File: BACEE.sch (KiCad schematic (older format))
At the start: 8 parts

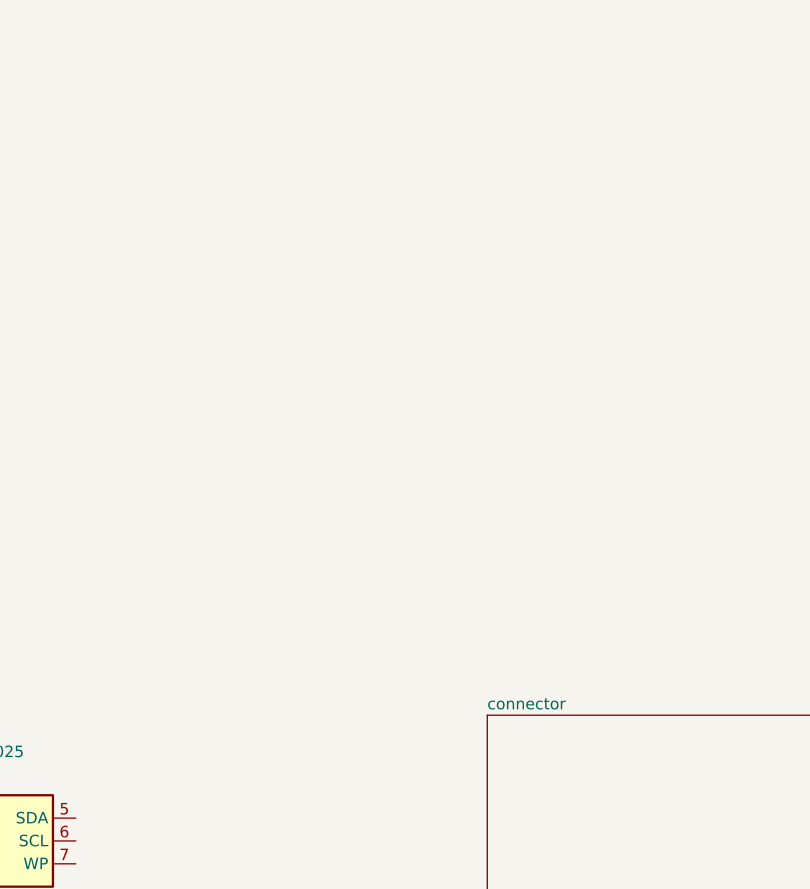
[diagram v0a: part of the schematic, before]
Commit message: created a new symbol
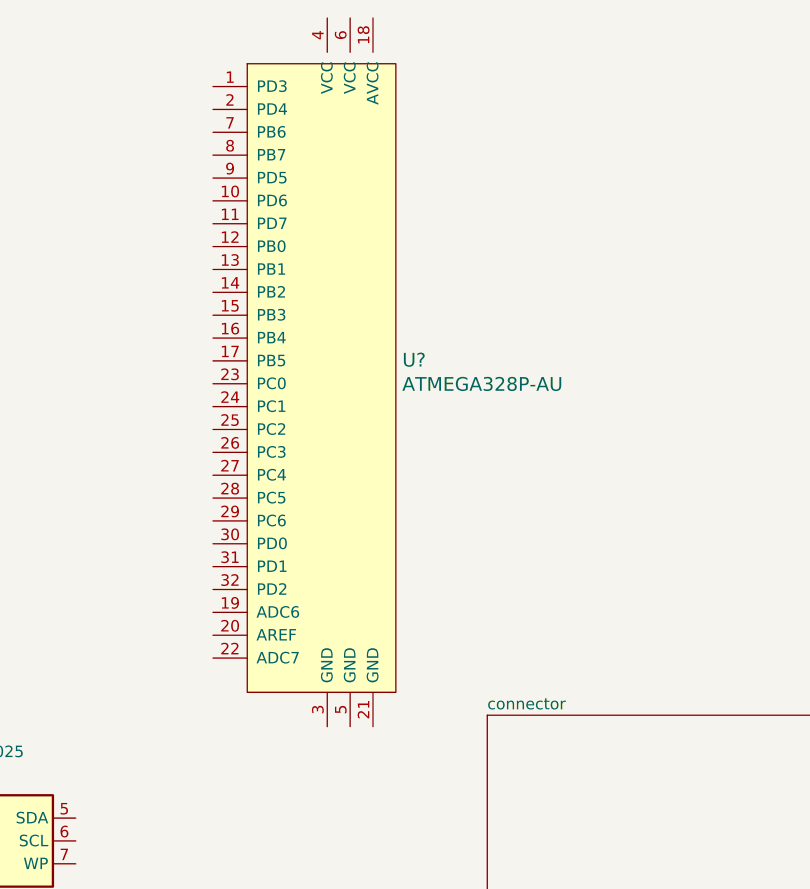
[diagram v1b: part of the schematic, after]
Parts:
- added U?: ATMEGA328P-AU, digikey-footprints:TQFP-32_7x7mm, symbol dk_Embedded-Microcontrollers:ATMEGA328P-AU
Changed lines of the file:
@@
 F1 "Connectors1.sch" 50
 $EndSheet
+$Comp
+L dk_Embedded-Microcontrollers:ATMEGA328P-AU U?
+U 1 1 5EFBB5FA
+P 7650 1750
+F 0 "U?" H 7978 1853 60  0000 L CNN
+F 1 "ATMEGA328P-AU" H 7978 1747 60  0000 L CNN
+F 2 "digikey-footprints:TQFP-32_7x7mm" H 7850 1950 60  0001 L CNN
+F 3 "http://www.microchip.com/mymicrochip/filehandler.aspx?ddocname=en608326" H 7850 2050 60  0001 L CNN
+F 4 "ATMEGA328P-AU-ND" H 7850 2150 60  0001 L CNN "Digi-Key_PN"
+F 5 "ATMEGA328P-AU" H 7850 2250 60  0001 L CNN "MPN"
+F 6 "Integrated Circuits (ICs)" H 7850 2350 60  0001 L CNN "Category"
+F 7 "Embedded - Microcontrollers" H 7850 2450 60  0001 L CNN "Family"
+F 8 "http://www.microchip.com/mymicrochip/filehandler.aspx?ddocname=en608326" H 7850 2550 60  0001 L CNN "DK_Datasheet_Link"
+F 9 "/product-detail/en/microchip-technology/ATMEGA328P-AU/ATMEGA328P-AU-ND/1832260" H 7850 2650 60  0001 L CNN "DK_Detail_Page"
+F 10 "IC MCU 8BIT 32KB FLASH 32TQFP" H 7850 2750 60  0001 L CNN "Description"
+F 11 "Microchip Technology" H 7850 2850 60  0001 L CNN "Manufacturer"
+F 12 "Active" H 7850 2950 60  0001 L CNN "Status"
+	1    7650 1750
+	1    0    0    -1
+$EndComp
 $EndSCHEMATC

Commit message: wiring done ... no DRC errors
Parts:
- added U2: 24LC1025, Package_SO:SOIJ-8_5.3x5.3mm_P1.27mm, symbol Memory_EEPROM:24LC1025
- added U3: DS1337_KTH, Package_SO:SO-8_5.3x6.2mm_P1.27mm, symbol Project_3_custom:DS1337_KTH
- added Y1: Crystal 32MHz, Crystal:Crystal_SMD_MicroCrystal_CC7V-T1A-2Pin_3.2x1.5mm, symbol Device:Crystal
- added Y2: Crystal 16MHz, Crystal:Crystal_SMD_5032-2Pin_5.0x3.2mm_HandSoldering, symbol Device:Crystal
- BT1: renamed from BT?; value Battery -> 3V; footprint (none) -> Connector_PinHeader_2.54mm:PinHeader_1x02_P2.54mm_Vertical
- C1, C2: renamed from C?; value C -> 22pF; footprint (none) -> Capacitor_SMD:C_0805_2012Metric_Pad1.15x1.40mm_HandSolder
- C3: renamed from C?; value CP -> 10uF; footprint (none) -> Capacitor_SMD:C_0805_2012Metric_Pad1.15x1.40mm_HandSolder
- D1: renamed from D?; footprint (none) -> LED_SMD:LED_0805_2012Metric_Pad1.15x1.40mm_HandSolder
- R1: renamed from R?; value R -> 330 ohms; footprint (none) -> Resistor_SMD:R_0805_2012Metric_Pad1.15x1.40mm_HandSolder
- R2: renamed from R?; value R -> 10k ohms; footprint (none) -> Resistor_SMD:R_0805_2012Metric_Pad1.15x1.40mm_HandSolder
- U1: renamed from U?; footprint (none) -> Package_SO:SOIJ-8_5.3x5.3mm_P1.27mm
- gave numbers to parts that had none: 1
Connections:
- net VCC: now reaches BT1.1 (+)
- net VCC: now also C3.1, R2.1, U1.3 (A2), U1.8 (VCC), U4.18 (AVCC), U4.20 (AREF), U4.4 (VCC), U4.6 (VCC), U2.3 (A2), U2.8 (VCC), U3.3 (INTA), U3.8 (Vcc)
- net GND: now reaches BT1.2 (-)
- net GND: now also C1.2, C2.2, C3.2, R1.2, U1.4 (GND), U1.7 (WP), U4.21 (GND), U4.3 (GND), U4.5 (GND), U2.4 (GND), U2.7 (WP), U3.4 (GND)
- net at C1.1: now also U4.7 (PB6), Y2.1
- net at C2.1: now also U4.8 (PB7), Y2.2
- net at D1.1 (K): now also R1.1
- net at D1.2 (A): now also U4.17 (PB5)
- net RST: now reaches R2.2
- net RST: now also U4.29 (PC6)
- net ADDS1: now reaches U1.1 (A0)
- net ADDS1: now also U4.23 (PC0), U2.1 (A0)
- net ADDS2: now reaches U1.2 (A1)
- net ADDS2: now also U4.24 (PC1), U2.2 (A1)
- net SDA: now reaches U1.5 (SDA)
- net SDA: now also U4.27 (PC4), U2.5 (SDA), U3.5 (SDA)
- net SCK: now reaches U1.6 (SCL)
- net SCK: now also U4.28 (PC5), U2.6 (SCL), U3.6 (SCL)
- net D3: now reaches U4.1 (PD3)
- net D6: now reaches U4.10 (PD6)
- net D7: now reaches U4.11 (PD7)
- net D8: now reaches U4.12 (PB0)
- net MOSI: now reaches U4.15 (PB3)
- net MISO: now reaches U4.16 (PB4)
- net D4: now reaches U4.2 (PD4)
- net RX: now reaches U4.30 (PD0)
- net TX: now reaches U4.31 (PD1)
- net D2: now reaches U4.32 (PD2)
- net D5: now reaches U4.9 (PD5)
- new net: U3.1 (X1), Y1.1
- new net: U3.2 (X2), Y1.2
- no-connect marks 0 -> 7
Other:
- moved on the sheet: BT1, C1, C2, C3, D1, R1, R2, U1, U4

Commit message: comments and netlist
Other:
- note added: "ATMEGA328P-AU with Oscilaltor and Battery"
- note added: "Clock/calender"
- note added: "Connectors"
- note added: "EPROM"
- moved on the sheet: BT1, C1, C2, C3, D1, R1, R2, U1, U2, U3, U4, Y1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

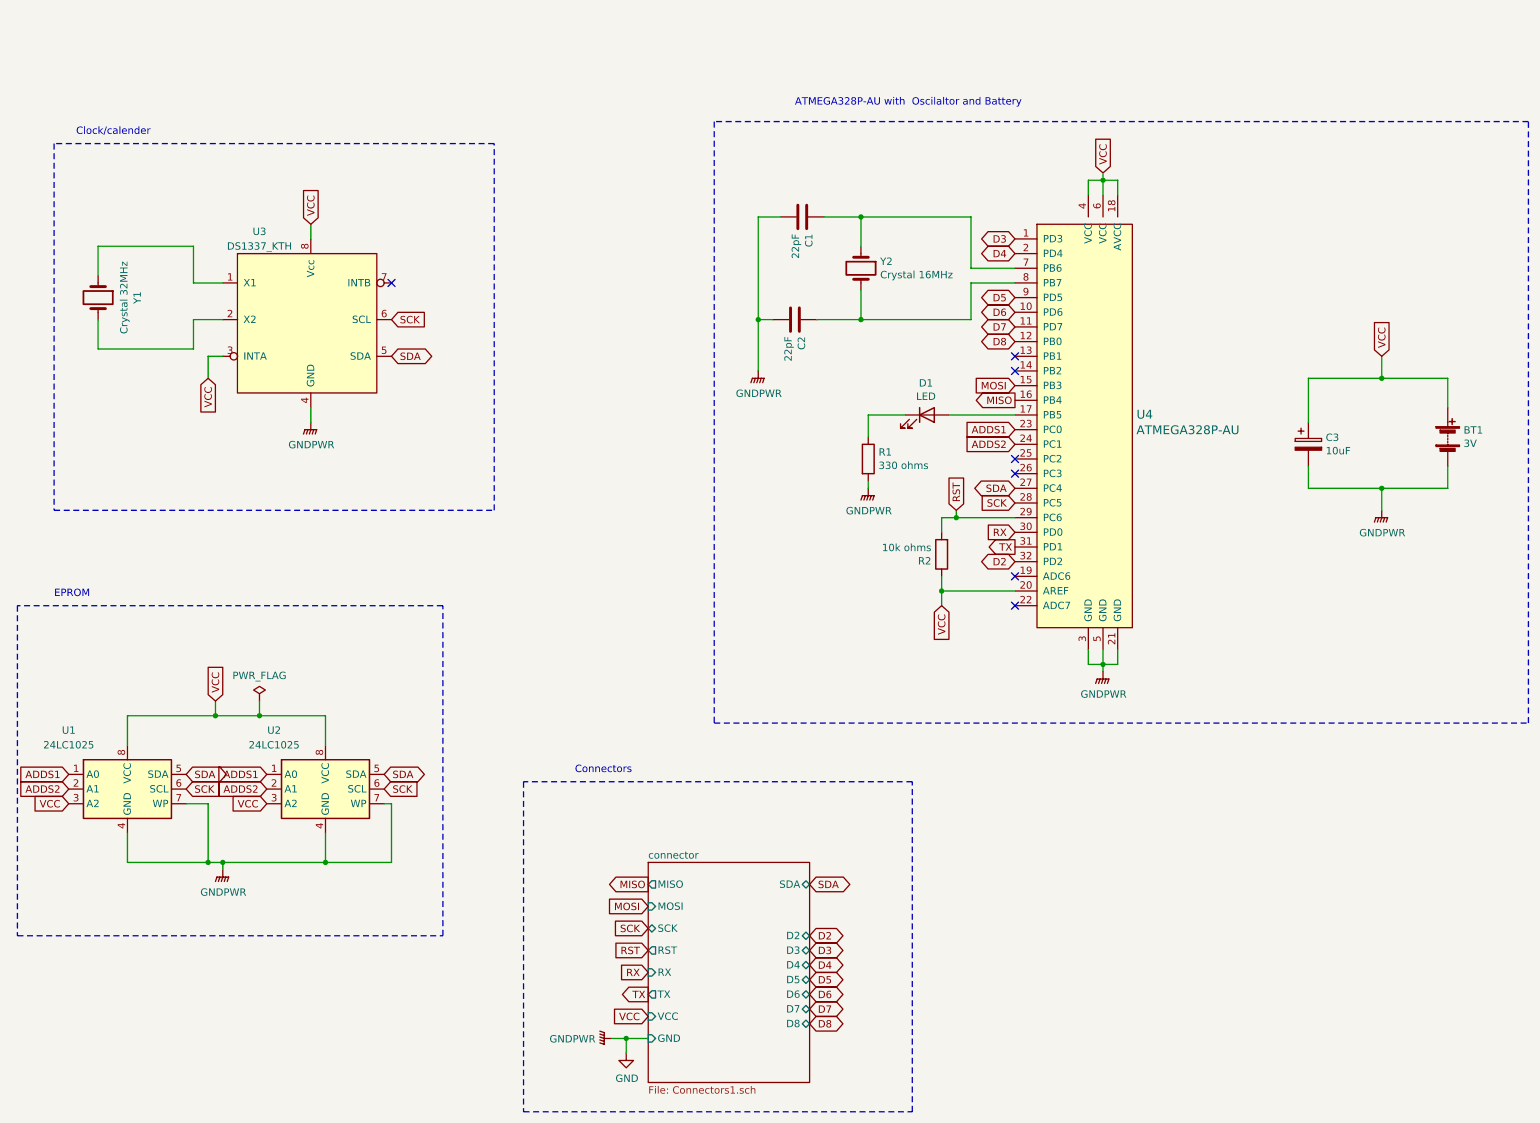
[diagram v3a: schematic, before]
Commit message: board layout with mounting holes
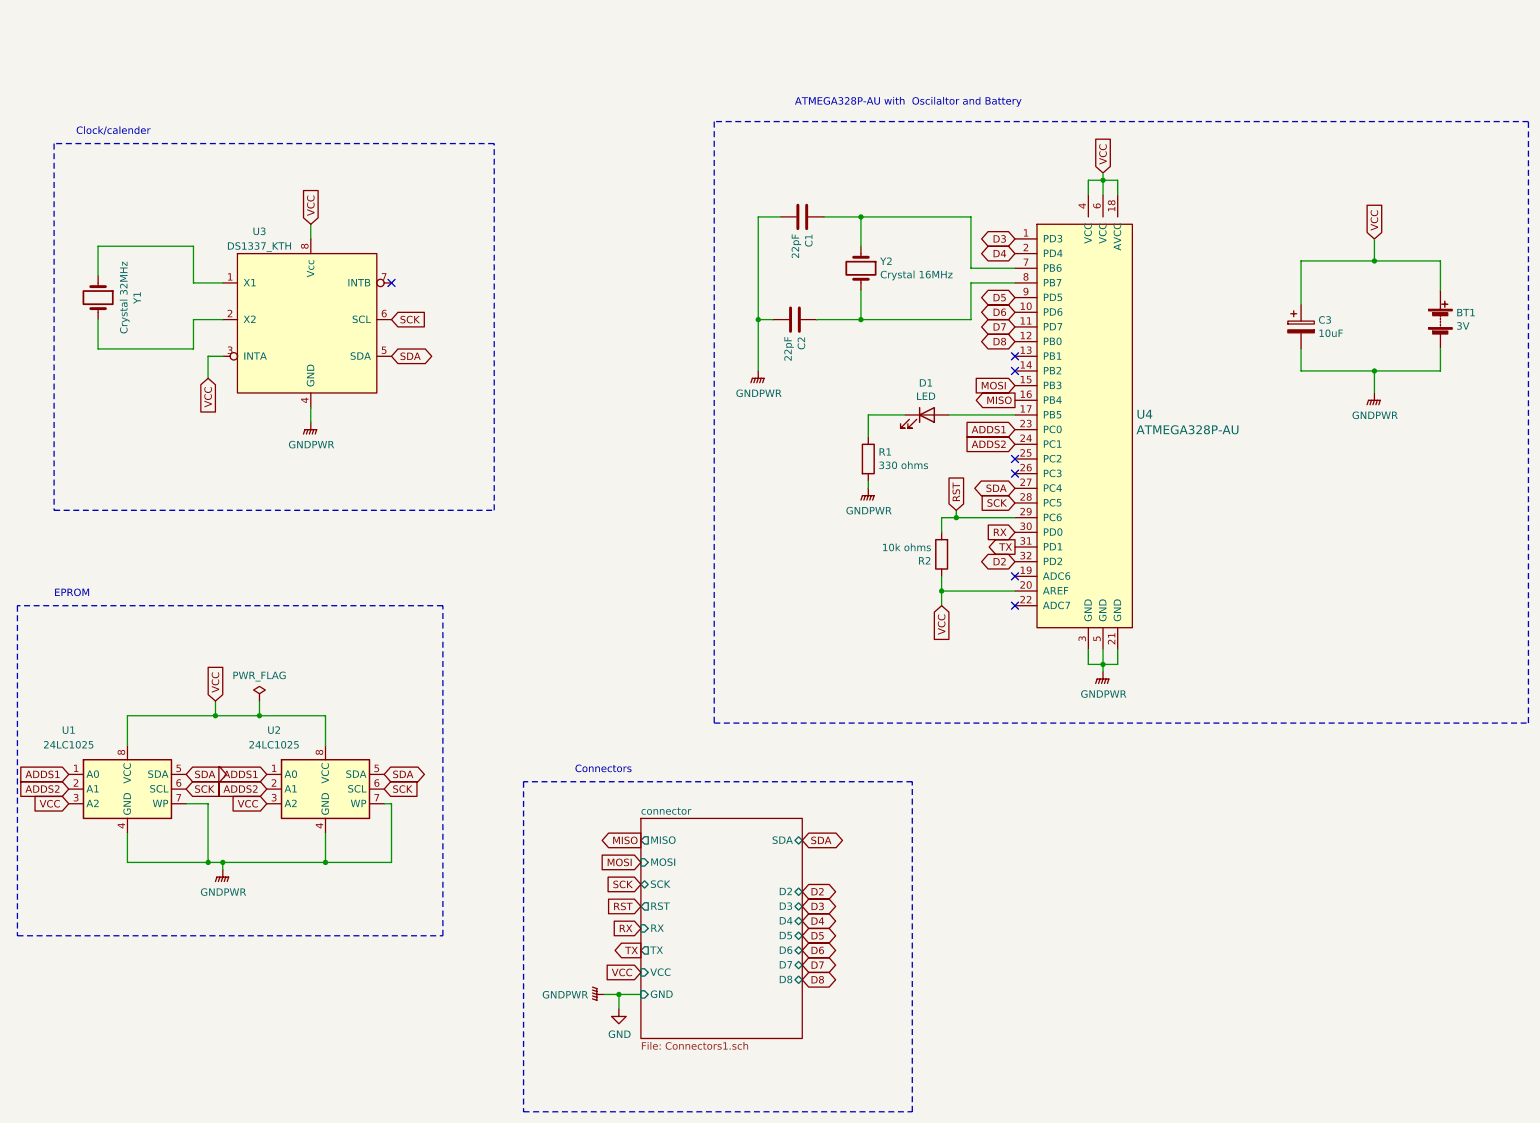
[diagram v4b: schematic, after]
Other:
- moved on the sheet: BT1, C3
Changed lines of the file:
@@
 L Device:CP C3
 U 1 1 5EFAFECC
-P 9500 3100
-F 0 "C3" H 9618 3146 50  0000 L CNN
-F 1 "10uF" H 9618 3055 50  0000 L CNN
-F 2 "Capacitor_SMD:C_0805_2012Metric_Pad1.15x1.40mm_HandSolder" H 9538 2950 50  0001 C CNN
-F 3 "~" H 9500 3100 50  0001 C CNN
-	1    9500 3100
+P 9450 2300
+F 0 "C3" H 9568 2346 50  0000 L CNN
+F 1 "10uF" H 9568 2255 50  0000 L CNN
+F 2 "Capacitor_SMD:C_0805_2012Metric_Pad1.15x1.40mm_HandSolder" H 9488 2150 50  0001 C CNN
+F 3 "~" H 9450 2300 50  0001 C CNN
+	1    9450 2300
 	1    0    0    -1
 $EndComp
@@
 	1    0    0    -1
 $EndComp
-Text GLabel 5000 6100 0    50   Output ~ 0
+Text GLabel 4950 5800 0    50   Output ~ 0
 MISO
 Text GLabel 7500 2800 0    50   Output ~ 0
 MISO
-Text GLabel 5000 6250 0    50   Input ~ 0
+Text GLabel 4950 5950 0    50   Input ~ 0
 MOSI
-Text GLabel 5000 6400 0    50   Input ~ 0
+Text GLabel 4950 6100 0    50   Input ~ 0
 SCK
-Text GLabel 5000 6550 0    50   Input ~ 0
+Text GLabel 4950 6250 0    50   Input ~ 0
 RST
-Text GLabel 5000 7000 0    50   Input ~ 0
+Text GLabel 4950 6700 0    50   Input ~ 0
 VCC
 Text GLabel 7500 2700 0    50   Input ~ 0
@@
 	8100 4600 8100 4650
 Wire Wire Line
-	4750 7150 4850 7150
+	4700 6850 4800 6850
 $Comp
 L power:GND #PWR02
 U 1 1 5EFF2D11
-P 4850 7250
-F 0 "#PWR02" H 4850 7000 50  0001 C CNN
-F 1 "GND" H 4855 7077 50  0000 C CNN
-F 2 "" H 4850 7250 50  0001 C CNN
-F 3 "" H 4850 7250 50  0001 C CNN
-	1    4850 7250
-	1    0    0    -1
-$EndComp
-Wire Wire Line
-	4850 7250 4850 7150
-Connection ~ 4850 7150
-Wire Wire Line
-	4850 7150 5000 7150
-Text GLabel 6100 6100 2    50   BiDi ~ 0
+P 4800 6950
+F 0 "#PWR02" H 4800 6700 50  0001 C CNN
+F 1 "GND" H 4805 6777 50  0000 C CNN
+F 2 "" H 4800 6950 50  0001 C CNN
+F 3 "" H 4800 6950 50  0001 C CNN
+	1    4800 6950
+	1    0    0    -1
+$EndComp
+Wire Wire Line
+	4800 6950 4800 6850
+Connection ~ 4800 6850
+Wire Wire Line
+	4800 6850 4950 6850
+Text GLabel 6050 5800 2    50   BiDi ~ 0
 SDA
-Text GLabel 6100 6450 2    50   BiDi ~ 0
+Text GLabel 6050 6150 2    50   BiDi ~ 0
 D2
-Text GLabel 6100 6550 2    50   BiDi ~ 0
+Text GLabel 6050 6250 2    50   BiDi ~ 0
 D3
-Text GLabel 6100 6650 2    50   BiDi ~ 0
+Text GLabel 6050 6350 2    50   BiDi ~ 0
 D4
-Text GLabel 6100 6750 2    50   BiDi ~ 0
+Text GLabel 6050 6450 2    50   BiDi ~ 0
 D5
-Text GLabel 6100 6850 2    50   BiDi ~ 0
+Text GLabel 6050 6550 2    50   BiDi ~ 0
 D6
-Text GLabel 6100 6950 2    50   BiDi ~ 0
+Text GLabel 6050 6650 2    50   BiDi ~ 0
 D7
-Text GLabel 6100 7050 2    50   BiDi ~ 0
+Text GLabel 6050 6750 2    50   BiDi ~ 0
 D8
-Text GLabel 5000 6700 0    50   Input ~ 0
+Text GLabel 4950 6400 0    50   Input ~ 0
 RX
-Text GLabel 5000 6850 0    50   Output ~ 0
+Text GLabel 4950 6550 0    50   Output ~ 0
 TX
 Text GLabel 7500 1700 0    50   BiDi ~ 0
@@
 L power:GNDPWR #PWR0101
 U 1 1 5F019B5C
-P 10000 3550
-F 0 "#PWR0101" H 10000 3350 50  0001 C CNN
-F 1 "GNDPWR" H 10004 3396 50  0000 C CNN
-F 2 "" H 10000 3500 50  0001 C CNN
-F 3 "" H 10000 3500 50  0001 C CNN
-	1    10000 3550
+P 9950 2750
+F 0 "#PWR0101" H 9950 2550 50  0001 C CNN
+F 1 "GNDPWR" H 9954 2596 50  0000 C CNN
+F 2 "" H 9950 2700 50  0001 C CNN
+F 3 "" H 9950 2700 50  0001 C CNN
+	1    9950 2750
 	1    0    0    -1
 $EndComp
@@
 L power:GNDPWR #PWR0104
 U 1 1 5F01DE34
-P 4750 7150
-F 0 "#PWR0104" H 4750 6950 50  0001 C CNN
-F 1 "GNDPWR" V 4754 7041 50  0000 R CNN
-F 2 "" H 4750 7100 50  0001 C CNN
-F 3 "" H 4750 7100 50  0001 C CNN
-	1    4750 7150
+P 4700 6850
+F 0 "#PWR0104" H 4700 6650 50  0001 C CNN
+F 1 "GNDPWR" V 4704 6741 50  0000 R CNN
+F 2 "" H 4700 6800 50  0001 C CNN
+F 3 "" H 4700 6800 50  0001 C CNN
+	1    4700 6850
 	0    1    1    0
 $EndComp
@@
 $EndComp
 Wire Wire Line
-	9500 3400 9500 3250
+	9450 2600 9450 2450
 $Comp
 L Device:Battery BT1
 U 1 1 5EFAD6D2
-P 10450 3050
-F 0 "BT1" H 10558 3096 50  0000 L CNN
-F 1 "3V" H 10558 3005 50  0000 L CNN
-F 2 "Connector_PinHeader_2.54mm:PinHeader_1x02_P2.54mm_Vertical" V 10450 3110 50  0001 C CNN
-F 3 "~" V 10450 3110 50  0001 C CNN
-	1    10450 3050
-	1    0    0    -1
-$EndComp
-Wire Wire Line
-	10450 3250 10450 3400
-Wire Wire Line
-	9500 2950 9500 2650
-Wire Wire Line
-	10450 2650 10450 2850
-Text GLabel 10000 2500 1    50   Input ~ 0
-VCC
-Wire Wire Line
-	9500 2650 10000 2650
-Wire Wire Line
-	9500 3400 10000 3400
-Wire Wire Line
-	10000 3550 10000 3400
-Connection ~ 10000 3400
-Wire Wire Line
-	10000 3400 10450 3400
-Wire Wire Line
-	10000 2650 10000 2500
-Connection ~ 10000 2650
-Wire Wire Line
-	10000 2650 10450 2650
+P 10400 2250
+F 0 "BT1" H 10508 2296 50  0000 L CNN
+F 1 "3V" H 10508 2205 50  0000 L CNN
+F 2 "Connector_PinHeader_2.54mm:PinHeader_1x02_P2.54mm_Vertical" V 10400 2310 50  0001 C CNN
+F 3 "~" V 10400 2310 50  0001 C CNN
+	1    10400 2250
+	1    0    0    -1
+$EndComp
+Wire Wire Line
+	10400 2450 10400 2600
+Wire Wire Line
+	9450 2150 9450 1850
+Wire Wire Line
+	10400 1850 10400 2050
+Text GLabel 9950 1700 1    50   Input ~ 0
+VCC
+Wire Wire Line
+	9450 1850 9950 1850
+Wire Wire Line
+	9450 2600 9950 2600
+Wire Wire Line
+	9950 2750 9950 2600
+Connection ~ 9950 2600
+Wire Wire Line
+	9950 2600 10400 2600
+Wire Wire Line
+	9950 1850 9950 1700
+Connection ~ 9950 1850
+Wire Wire Line
+	9950 1850 10400 1850
 Wire Wire Line
 	7500 1900 7200 1900
@@
 	2350 4950 2800 4950
 $Sheet
-S 5000 5950 1100 1500
+S 4950 5650 1100 1500
 U 5EFB4B62
 F0 "connector" 50
 F1 "Connectors1.sch" 50
-F2 "SCK" B L 5000 6400 50
-F3 "RST" O L 5000 6550 50
-F4 "VCC" I L 5000 7000 50
-F5 "MOSI" I L 5000 6250 50
-F6 "GND" I L 5000 7150 50
-F7 "RX" I L 5000 6700 50
-F8 "TX" O L 5000 6850 50
-F9 "SDA" B R 6100 6100 50
-F10 "D2" B R 6100 6450 50
-F11 "D3" B R 6100 6550 50
-F12 "D4" B R 6100 6650 50
-F13 "D5" B R 6100 6750 50
-F14 "D6" B R 6100 6850 50
-F15 "D8" B R 6100 7050 50
-F16 "D7" B R 6100 6950 50
-F17 "MISO" O L 5000 6100 50
+F2 "SCK" B L 4950 6100 50
+F3 "RST" O L 4950 6250 50
+F4 "VCC" I L 4950 6700 50
+F5 "MOSI" I L 4950 5950 50
+F6 "GND" I L 4950 6850 50
+F7 "RX" I L 4950 6400 50
+F8 "TX" O L 4950 6550 50
+F9 "SDA" B R 6050 5800 50
+F10 "D2" B R 6050 6150 50
+F11 "D3" B R 6050 6250 50
+F12 "D4" B R 6050 6350 50
+F13 "D5" B R 6050 6450 50
+F14 "D6" B R 6050 6550 50
+F15 "D8" B R 6050 6750 50
+F16 "D7" B R 6050 6650 50
+F17 "MISO" O L 4950 5800 50
 $EndSheet
 Wire Notes Line
